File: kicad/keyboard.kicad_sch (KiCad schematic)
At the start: 7 parts, among them J7 KBD, U127 74LS125, U141 74LS74, U142 74LS299, U150 PAL20L8

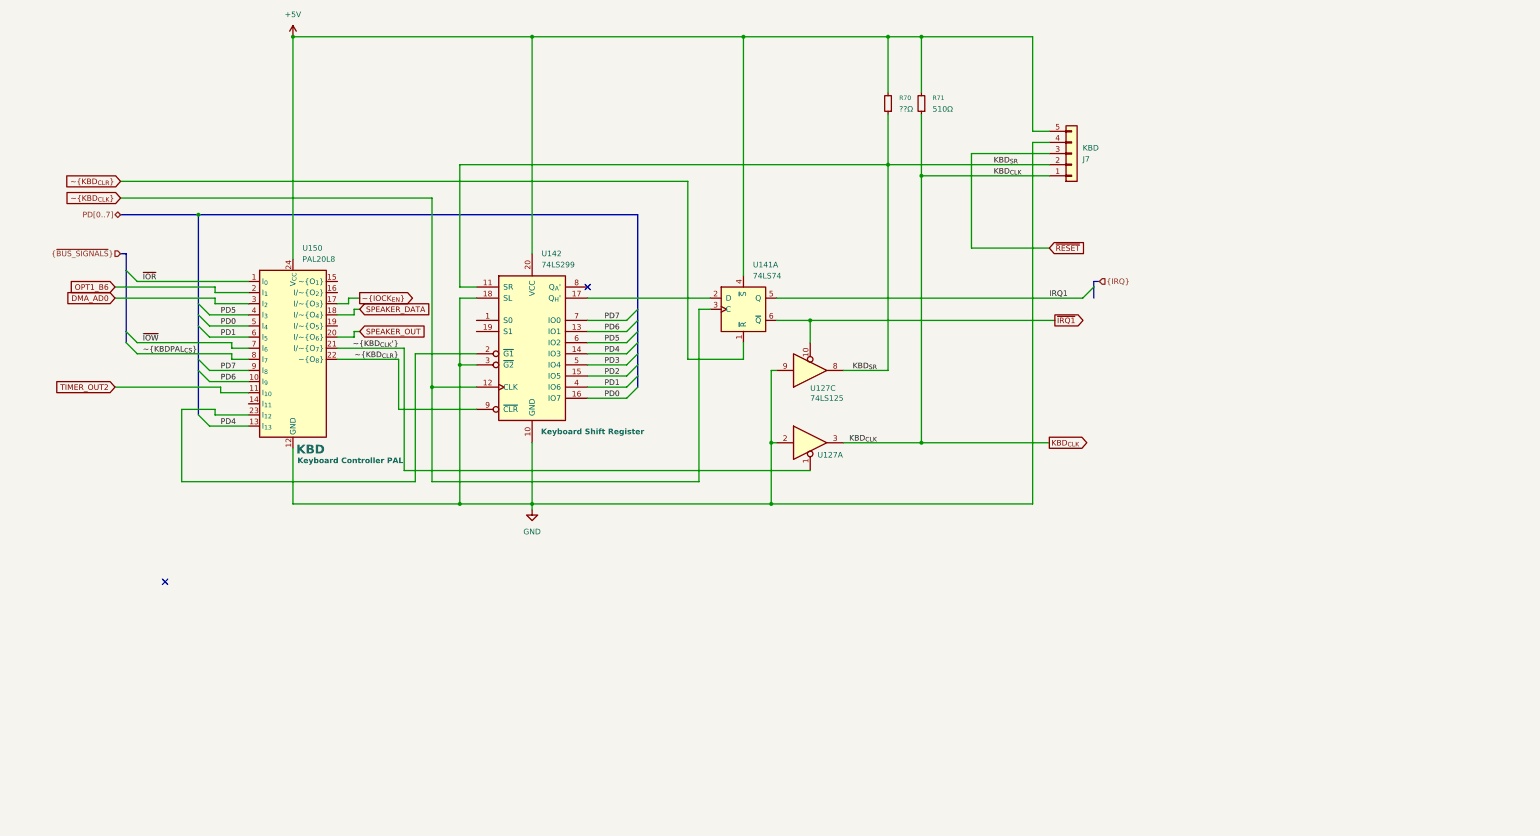
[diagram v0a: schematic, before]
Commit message: Fixes to clocks,  keyboard controller stuff.
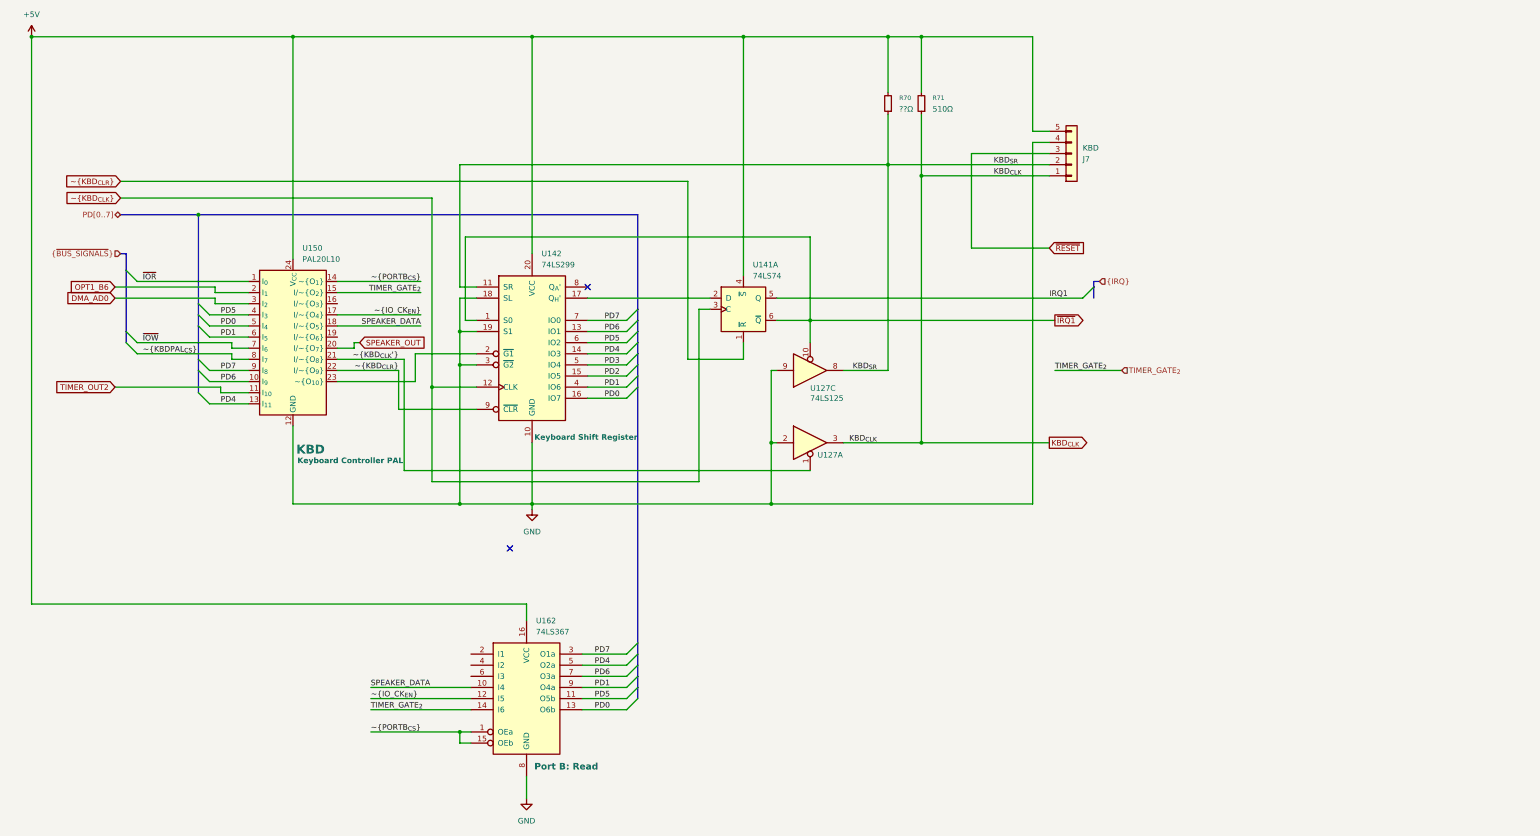
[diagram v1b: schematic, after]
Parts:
- added U162: 74LS367, Package_DIP:DIP-16_W7.62mm, symbol 74xx:74LS367
- U150: value PAL20L8 -> PAL20L10; symbol Logic_Programmable:PAL20L8 -> seequa:PAL20L10
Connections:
- net +5V: now also U162.16 (VCC)
- net GND: now also U142.19 (S1), U162.8 (GND)
- net PD0: now also U162.13 (O6b)
- net PD1: now also U162.9 (O4a)
- net PD4: now also U162.5 (O2a)
- net PD5: now also U162.11 (O5b)
- net PD6: now also U162.7 (O3a)
- net PD7: now also U162.3 (O1a)
- net SPEAKER_DATA: now also U162.10 (I4)
- net ~{IRQ1}: now also U142.1 (S0)
- net ~{PORTB_{CS}}: now reaches U150.14 (~{O_{1}})
- net ~{PORTB_{CS}}: now also U162.1 (OEa), U162.15 (OEb)
- net TIMER_GATE_{2}: now reaches U150.15 (I/~{O_{2}})
- net TIMER_GATE_{2}: now also U162.14 (I6)
- net ~{IOCK_{EN}} renamed ~{IO_CK_{EN}}
- net ~{IO_CK_{EN}}: now also U162.12 (I5)
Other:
- moved on the sheet: U150

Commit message: update kicad project
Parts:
- added C84, C85: C_Bypass_5mm, seequa_footprints:C_Seequa_Bypass_Film_5mm, symbol seequa:C_Bypass_Film_2.54mm
- added U82: 74LS00, Package_DIP:DIP-14_W7.62mm, symbol 74xx:74LS00
- J7: seq_coord (none) -> M28; seq_silkscreen (none) -> J7
- R70: seq_coord (none) -> M30
- R71: seq_coord (none) -> M30; seq_silkscreen R40 -> R71
- U127: seq_coord (none) -> J16; seq_silkscreen (none) -> LS125
- U141: seq_coord (none) -> I15; seq_silkscreen (none) -> LS74
- U142: seq_coord (none) -> I14
- U150: seq_coord (none) -> I12
- U162: seq_coord (none) -> D21
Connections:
- net ~{KBD_{CLK}'} is gone; now on net ~{KBD_CLK_{PD}}: U127.1, U150.21 (I/~{O_{8}})
- net ~{KBD_{CLR}}: now also U82.12, U82.13
- net ~{BRD_CK_{EN}}: now reaches U150.16 (I/~{O_{3}})
- net ~{BRD_CK_{EN}}: now also U162.4 (I2)
- net KBD_{CLR}: now reaches U142.2 (~{G1}), U150.23 (~{O_{10}})
- net KBD_{CLR}: now also U162.2 (I1), U82.11
- net at U142.8 (Q_{A}'): no longer names the net of U142.8 (Q_{A}')
- net ~{KBD_CLK_{PD}}: now reaches U162.6 (I3)
- net DMA_AD0 renamed XAT0
- net KBD_{SR} renamed KBD_{DATA}
- net TIMER_OUT2 renamed TIMER_OUT_{2}
- net ~{KBD_{CLK}} renamed ~{KBD_SHIFT_{CLK}}
- net ~{RESET} renamed ~{RESET_{BRD}}
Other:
- moved on the sheet: J7, R70, R71, U127A, U127C, U141A, U142, U162

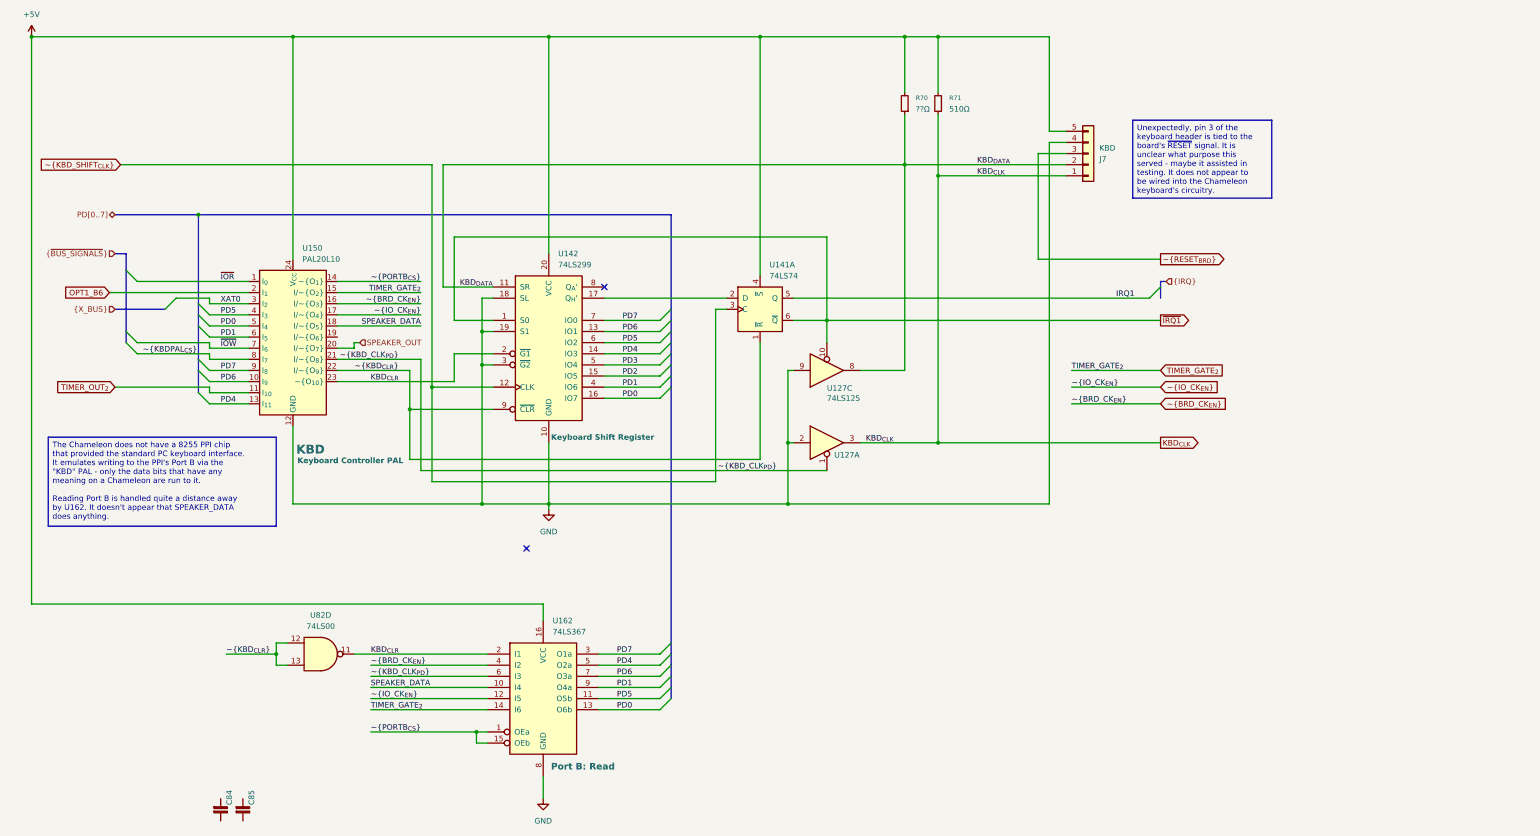
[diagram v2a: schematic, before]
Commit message: Add parallel port, game port
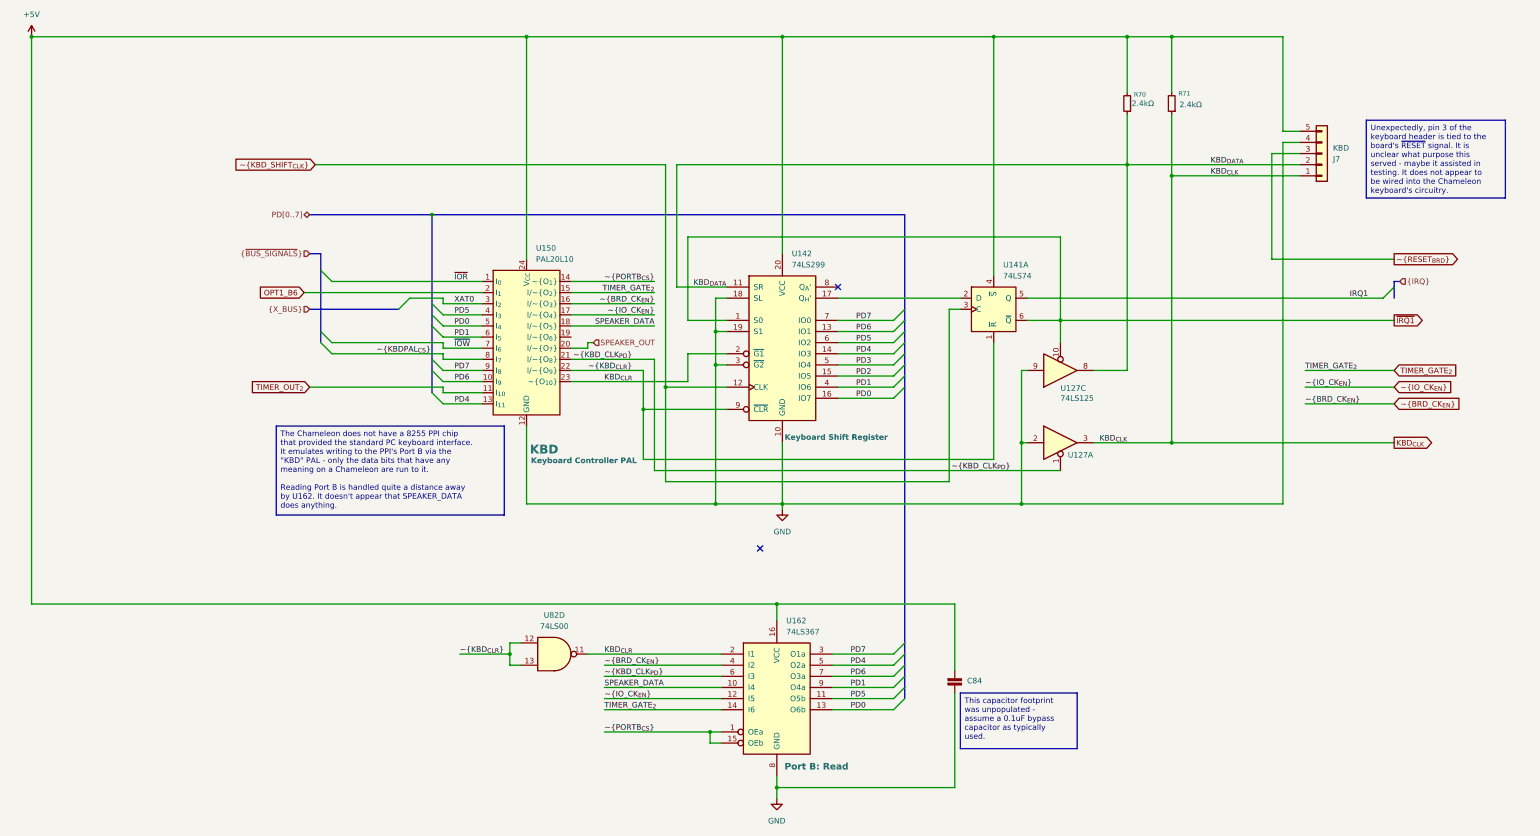
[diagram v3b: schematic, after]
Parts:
- removed C85: C_Bypass_5mm, seequa_footprints:C_Seequa_Bypass_Film_5mm, symbol seequa:C_Bypass_Film_2.54mm
- R70: value ??Ω -> 2.4kΩ
- R71: value 510Ω -> 2.4kΩ; seq_notes Green,Black,Black,Gold -> Red, Yellow, Red, Gold
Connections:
- net +5V: now also C84.1
- net GND: now also C84.2
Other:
- moved on the sheet: C84, J7, R70, R71, U127A, U127C, U141A, U142, U150, U162, U82D
